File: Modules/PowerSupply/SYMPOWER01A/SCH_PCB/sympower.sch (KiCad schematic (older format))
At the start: 13 parts

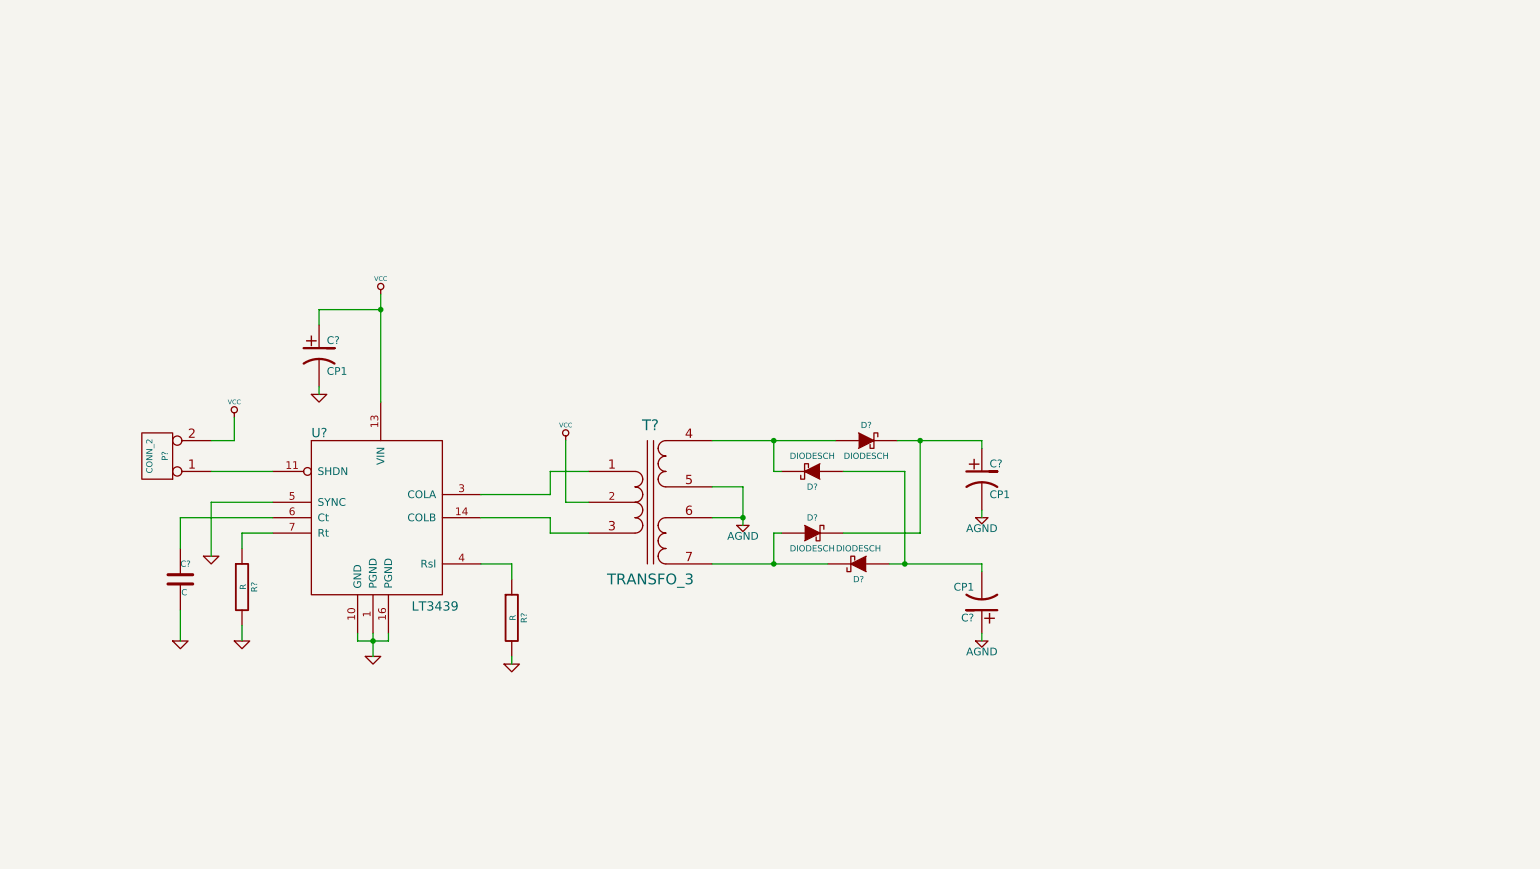
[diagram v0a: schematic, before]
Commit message: pridano schema symetrickeho zdroje..
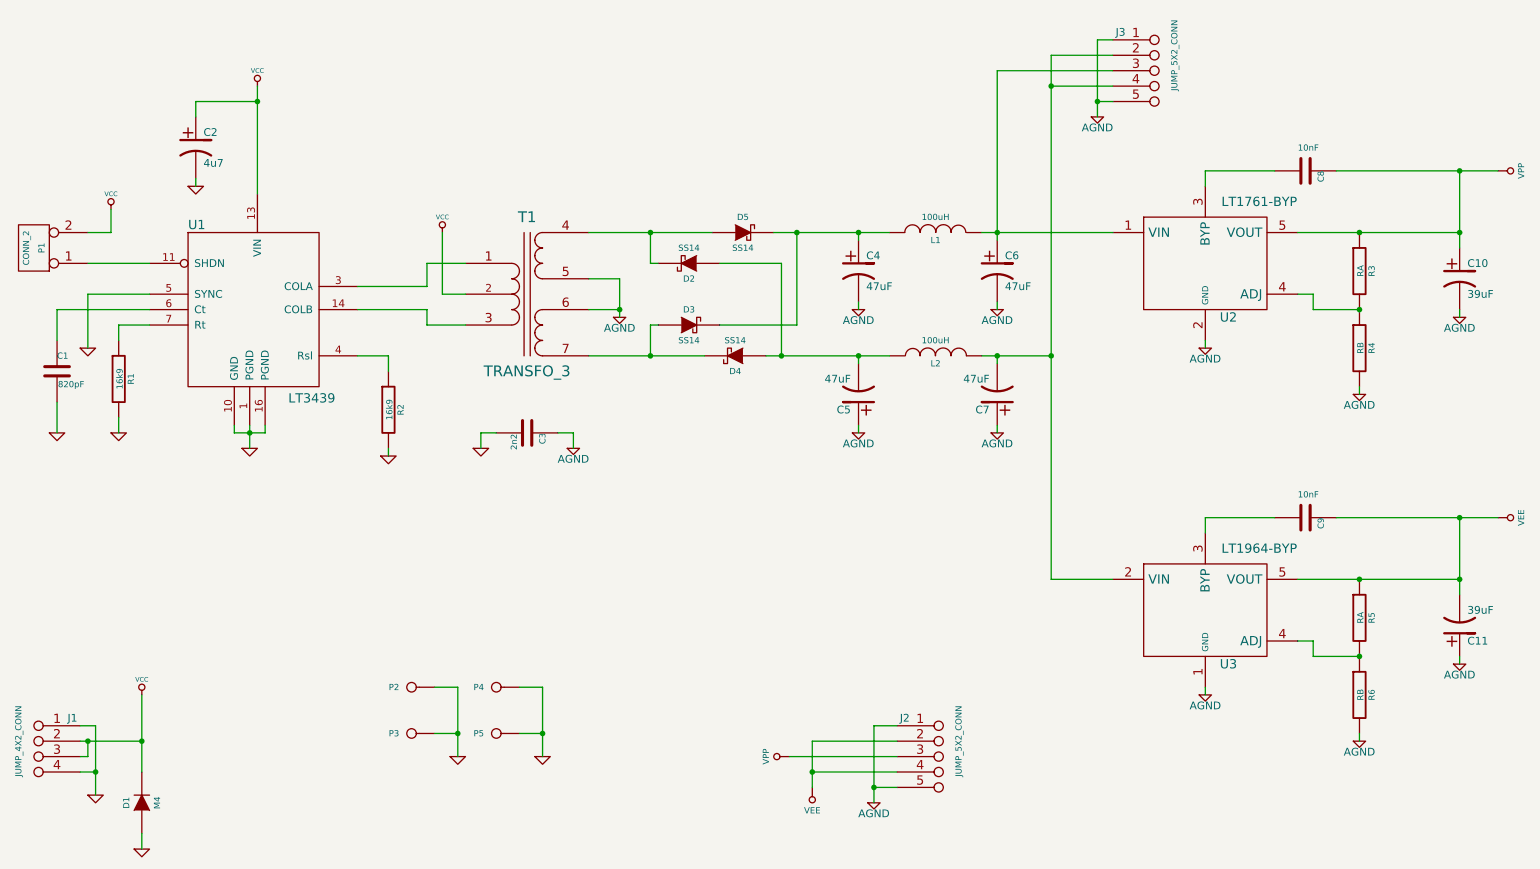
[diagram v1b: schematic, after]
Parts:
- added C10, C11: 39uF, symbol CP1
- added C3: 2n2, symbol C
- added C6, C7: 47uF, symbol CP1
- added C8, C9: 10nF, symbol C
- added D1: M4, symbol DIODE
- added J1: JUMP_4X2_CONN, symbol JUMP_4X2_CONN
- added J2, J3: JUMP_5X2_CONN, symbol JUMP_5X2_CONN
- added L1, L2: 100uH, symbol INDUCTOR
- added P2, P3, P4, P5: CONN_1, symbol CONN_1
- added R3, R5: RA, symbol R
- added R4, R6: RB, symbol R
- added U2: LT1761-BYP, symbol LT1761-BYP
- added U3: LT1964-BYP, symbol LT1964-BYP
- C1: renamed from C?; value C -> 820pF
- C2: renamed from C?; value CP1 -> 4u7
- C4, C5: renamed from C?; value CP1 -> 47uF
- D2, D3, D4, D5: renamed from D?; value DIODESCH -> SS14
- R1, R2: renamed from R?; value R -> 16k9
- gave numbers to parts that had none: 3
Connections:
- net AGND: now also C10.2, C11.1, C3.1, C6.2, C7.1, J2.1, J2.10, J2.5, J2.6, J3.1, J3.10, J3.5, J3.6, R4.2, R6.2, U2.2 (GND), U3.1 (GND)
- net GND: now also C3.2, D1.1 (A), J1.1, J1.4, J1.5, J1.8, P2.1, P3.1, P4.1, P5.1
- net VCC: now also D1.2 (K), J1.2 (1), J1.3, J1.6, J1.7
- net at C4.1, D3.2 (K), D5.2 (K): now also L1.2
- net at C5.2, D2.1 (A), D4.1 (A): now also L2.1
- new net: C6.1, J3.3, J3.8, L1.1, U2.1 (VIN)
- new net: C7.2, J3.2 (1), J3.4, J3.7, J3.9, L2.2, U3.2 (VIN)
- new net: C8.2, U2.3 (BYP)
- new net: R3.2, R4.1, U2.4 (ADJ)
- new net: C9.2, U3.3 (BYP)
- new net: R5.2, R6.1, U3.4 (ADJ)
- new net VEE: C11.2, C9.1, J2.2 (1), J2.4, J2.7, J2.9, R5.1, U3.5 (VOUT)
- new net VPP: C10.1, C8.1, J2.3, J2.8, R3.1, U2.5 (VOUT)
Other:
- moved on the sheet: C1, C2, C4, C5, D2, D3, D4, D5, P1, R1, R2, T1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
